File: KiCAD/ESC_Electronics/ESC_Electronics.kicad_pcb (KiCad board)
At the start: 2 copper layers, 57 parts, among them J1 -1000VDC, J2 Test Input, J3 CA probe, J4 DC Power, J5 Output, J6 Barrel_Jack, Q1 MMBT3906, Q2 MMBT3904, U1 CR110, U2 SiPhotodiode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

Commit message: laying out V1
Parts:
- added H1: MountingHole, MountingHole:MountingHole_3.2mm_M3, F.Cu at (195.6, 66.0)
- added H2: MountingHole, MountingHole:MountingHole_3.2mm_M3, F.Cu at (195.6, 124.5)
- added H3: MountingHole, MountingHole:MountingHole_3.2mm_M3, F.Cu at (79.0, 63.2)
- added H4: MountingHole, MountingHole:MountingHole_3.2mm_M3, F.Cu at (55.9, 124.5)
- added J7: -6V, Connector_PinHeader_2.54mm:PinHeader_1x02_P2.54mm_Vertical, F.Cu at (108.2, 120.6)
- added J8: +6V, Connector_PinHeader_2.54mm:PinHeader_1x02_P2.54mm_Vertical, F.Cu at (108.2, 106.4)
- added TH1: PTC 200mA, Fuse:Fuse_1210_3225Metric_Pad1.42x2.65mm_HandSolder, F.Cu at (64.8, 96.8)
- moved R4 115.4 mm to (133.6, 106.2)
- moved C4 111.7 mm to (74.2, 83.3), turned to 90 degrees
- moved R3 102.9 mm to (133.6, 101.1)
- moved BT6 97.4 mm to (136.4, 117.3), turned to 180 degrees
- moved R5 86.4 mm to (146.3, 70.6), turned to 0 degrees
- moved J4 85.4 mm to (84.5, 119.3), turned to 180 degrees
- moved D2 81.4 mm to (91.7, 121.7), turned to 0 degrees
- moved D1 79.7 mm to (91.7, 116.3), turned to 180 degrees
- moved R8 77.8 mm to (146.3, 65.7), turned to 0 degrees
- moved BT2 77.2 mm to (185.9, 91.7), turned to 90 degrees
- moved J3 71.6 mm to (93.2, 64.0), turned to -90 degrees
- moved U2 69.3 mm to (132.1, 84.6), turned to -90 degrees
- moved D5 67.9 mm to (103.1, 113.0)
- moved R6 66.6 mm to (131.1, 65.5), turned to 0 degrees
- moved BT5 65.3 mm to (171.4, 91.7), turned to 90 degrees
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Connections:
- L1 pad 1: Net-(J6-Pad1) -> Net-(L1-Pad1)
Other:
- rule pad_to_mask_clearance: 0 -> 0.0508
- board text added: "HV"
- board text added: "Output"
- board text added: "Test"

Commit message: layed out board
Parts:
- added H5: DiodeFeedThru, ESC_Electronics_Library:DiodeFeedThru, F.Cu at (118.7, 89.4)
- added R20: 10k, Resistor_THT:R_Axial_DIN0207_L6.3mm_D2.5mm_P5.08mm_Vertical, F.Cu at (108.0, 77.0)
- C6: value 1nF -> 1pF
- R11: footprint Resistor_SMD:R_0805_2012Metric_Pad1.20x1.40mm_HandSolder -> Resistor_THT:R_Axial_DIN0207_L6.3mm_D2.5mm_P5.08mm_Vertical
- R12: value 20k -> 10k; footprint Resistor_SMD:R_0805_2012Metric_Pad1.20x1.40mm_HandSolder -> Resistor_THT:R_Axial_DIN0207_L6.3mm_D2.5mm_P5.08mm_Vertical
- moved R11 6.66 mm to (93.5, 79.5), turned to -90 degrees
- moved R12 6.38 mm to (98.0, 77.0), turned to 0 degrees
- moved H1 6.04 mm to (195.5, 60.0)
- moved H3 4.24 mm to (77.0, 59.5)
- moved C12 3.42 mm to (103.1, 103.0)
- moved R18 2.62 mm to (103.1, 106.5)
- moved U3 1.52 mm to (106.4, 83.3)
- moved C9 1.13 mm to (105.5, 94.0)
- moved D6 0.71 mm to (103.2, 99.5)
- moved D5 0.47 mm to (103.1, 113.5)
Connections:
- C9 pad 2: Net-(C9-Pad2) -> GND
- R12 pad 1: Net-(J5-Pad1) -> GND
- R12 pad 2: Net-(R11-Pad2) -> Net-(R12-Pad2)
- U3 pad 2: Net-(C9-Pad2) -> Net-(R12-Pad2)
- U3 pad 4: Net-(C9-Pad2) -> GND
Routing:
- net Net-(R3-Pad2): track 0.00 -> 96.5 mm
- net Net-(C2-Pad1): track 0.00 -> 80.2 mm
- net -6VDC: track 0.00 -> 70.4 mm, vias 0 -> 2
- net Net-(C10-Pad2): track 0.00 -> 69.9 mm, vias 0 -> 1
- net +6VDC: track 0.00 -> 62.2 mm
- net Net-(BT2-Pad1): track 0.00 -> 42.8 mm
- net Net-(C10-Pad1): track 0.00 -> 40.5 mm
- net Net-(BT1-Pad2): track 0.00 -> 39.2 mm
- net Net-(BT2-Pad2): track 0.00 -> 37.7 mm
- net Net-(BT1-Pad1): track 0.00 -> 37.7 mm
- net Net-(BT3-Pad1): track 0.00 -> 37.7 mm
- net Net-(C5-Pad1): track 0.00 -> 36.3 mm
- net Net-(C8-Pad1): track 0.00 -> 26.7 mm
- net Net-(J5-Pad1): track 0.00 -> 23.3 mm
- net Net-(D1-Pad1): track 0.00 -> 22.8 mm, vias 0 -> 2
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- added copper zone on B.Cu, net GND
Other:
- board outline added: 149.5 x 74.5 mm
- board text added: "+6V GND"
- board text added: "+8V GND -8V"
- board text added: "-6V GND"
- board text added: "100uH"
- board text added: "1uF"
- board text added: "200mA PTC"
- board text added: "24VDC -Floating+"
- board text added: "BIAS IN"
- board text added: "GND"
- board text added: "LM317"
- board text added: "PreAmp Output"
- board text added: "TL072"
- board text added: "TLE2426"

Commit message: uploaded this version to OSHpark as V1
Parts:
- added H6: MountingHole, ESC_Electronics_Library:4headclear, F.Cu at (118.7, 108.4)
- added H7: MountingHole, ESC_Electronics_Library:4headclear, F.Cu at (118.7, 70.3)
- C1, C4: footprint Capacitor_SMD:C_1206_3216Metric_Pad1.33x1.80mm_HandSolder -> Capacitor_SMD:C_0805_2012Metric_Pad1.18x1.45mm_HandSolder
- R18, R19: footprint Resistor_SMD:R_0805_2012Metric_Pad1.20x1.40mm_HandSolder -> Resistor_SMD:R_1206_3216Metric_Pad1.30x1.75mm_HandSolder
- moved R6 6.37 mm to (136.9, 63.0)
- moved C7 5.51 mm to (134.1, 70.1)
- moved C3 5.20 mm to (126.5, 63.5)
- moved BT4 3.05 mm to (173.2, 120.4)
- moved BT6 3.05 mm to (136.4, 120.4)
- moved R5 2.03 mm to (148.3, 70.6)
- moved R8 2.03 mm to (148.3, 65.7)
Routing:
- net Net-(BT1-Pad2): track 39.2 -> 45.7 mm
- net Net-(C2-Pad1): track 80.2 -> 84.5 mm
- net Net-(BT2-Pad1): track 42.8 -> 45.9 mm
- net Net-(R3-Pad2): track 96.5 -> 99.2 mm
- net Net-(C5-Pad1): track 36.3 -> 34.2 mm
- net Net-(J1-Pad1): track 8.39 -> 6.36 mm
- net Net-(C3-Pad2): track 4.32 -> 5.58 mm
- net Net-(BT6-Pad1): track 19.9 -> 21.1 mm
- net Net-(D2-Pad2): track 16.1 -> 15.3 mm
- net Net-(D1-Pad1): track 22.8 -> 22.3 mm
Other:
- board text added: "Input Only"

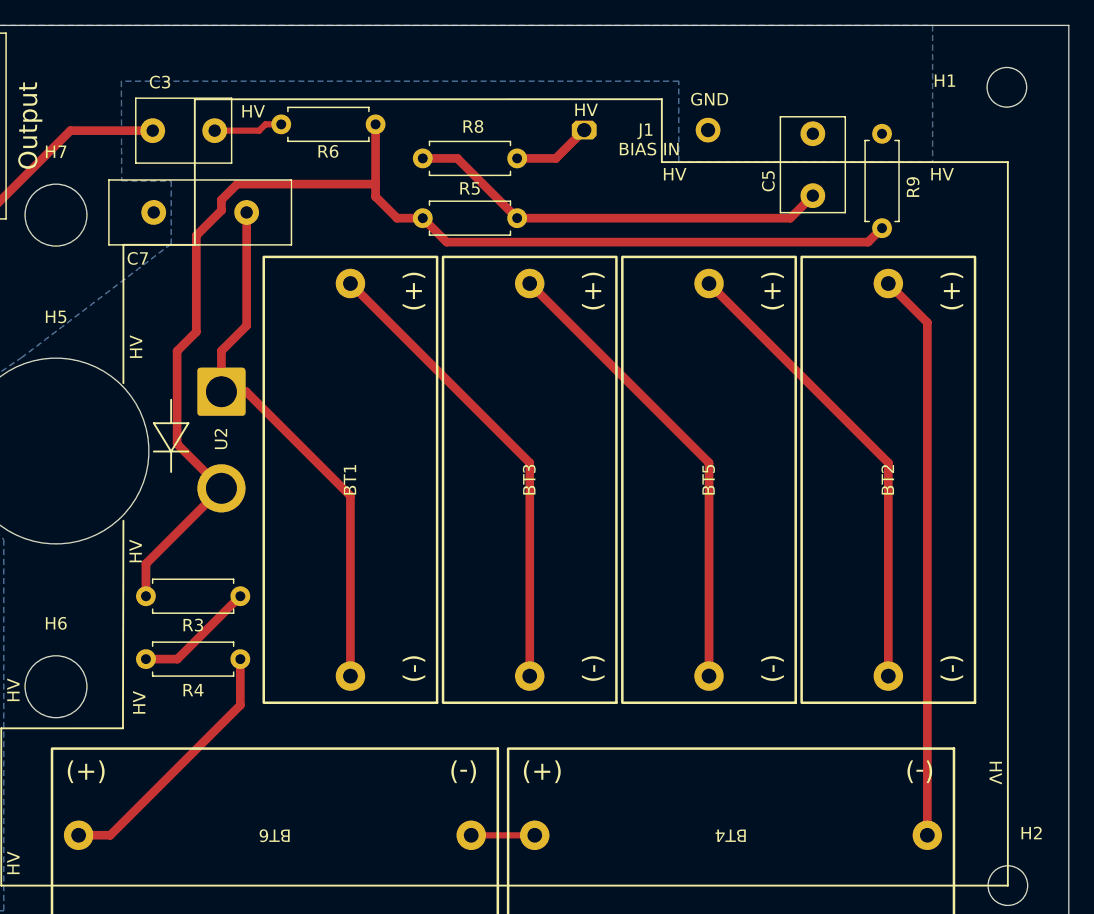
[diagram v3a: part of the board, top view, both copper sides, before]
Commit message: the real ESC V1
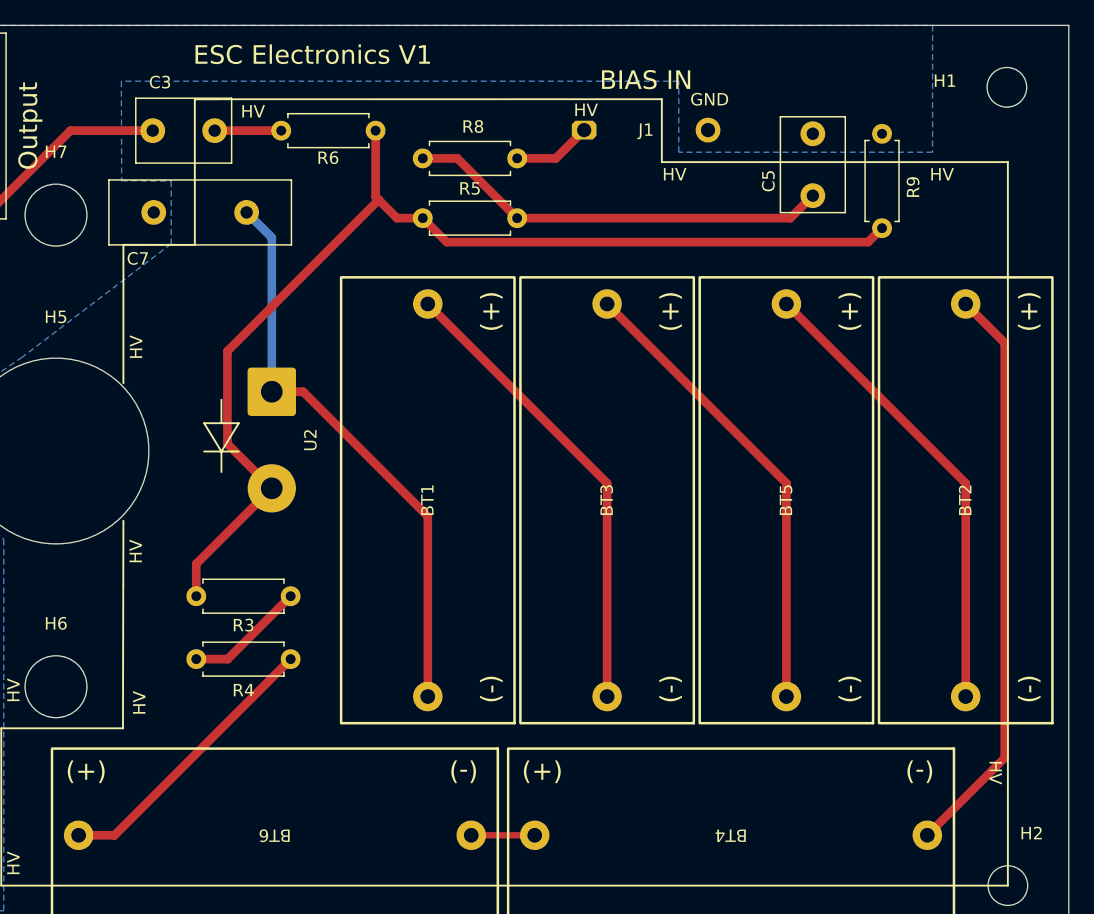
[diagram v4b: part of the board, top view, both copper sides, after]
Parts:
- U2: footprint Connector_Wire:SolderWire-2sqmm_1x02_P7.8mm_D2mm_OD3.9mm -> Connector_Wire:SolderWire-1sqmm_1x02_P7.8mm_D1.4mm_OD3.9mm
- moved BT5 6.46 mm to (177.7, 93.3)
- moved BT1 6.46 mm to (148.7, 93.3)
- moved BT2 6.46 mm to (192.2, 93.3)
- moved BT3 6.46 mm to (163.2, 93.3)
- moved R3 4.06 mm to (137.7, 101.1)
- moved R4 4.06 mm to (137.7, 106.2)
- moved U2 4.06 mm to (136.1, 84.6)
- moved R6 0.51 mm to (136.9, 63.5)
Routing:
- net Net-(R3-Pad2): track 99.2 -> 89.3 mm
- net Net-(BT1-Pad2): track 45.7 -> 48.6 mm
- net Net-(BT6-Pad1): track 21.1 -> 23.0 mm
- net Net-(BT2-Pad1): track 45.9 -> 46.8 mm
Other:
- board text added: "ESC Electronics V1"

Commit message: Refining for V2 while debugging
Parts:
- added C13: 0.1uF, Capacitor_SMD:C_0805_2012Metric_Pad1.18x1.45mm_HandSolder, F.Cu at (87.5, 97.0)
- D5, D6: value MM3Z6V8 -> MM3Z7V5T1G
- J6: footprint Connector_Wire:SolderWire-0.75sqmm_1x02_P7mm_D1.25mm_OD3.5mm -> Connector_Wire:SolderWire-0.25sqmm_1x02_P4.2mm_D0.65mm_OD1.7mm
- R11, R12, R20: footprint Resistor_THT:R_Axial_DIN0207_L6.3mm_D2.5mm_P5.08mm_Vertical -> Resistor_THT:R_Axial_DIN0207_L6.3mm_D2.5mm_P10.16mm_Horizontal
- U2: footprint Connector_Wire:SolderWire-1sqmm_1x02_P7.8mm_D1.4mm_OD3.9mm -> Connector_Wire:SolderWire-0.25sqmm_1x02_P4.2mm_D0.65mm_OD1.7mm
- moved U5 20.7 mm to (82.5, 116.0)
- moved R20 17.9 mm to (90.4, 80.5)
- moved D1 15.7 mm to (78.0, 124.0)
- moved D2 14.5 mm to (78.0, 126.5)
- moved J4 14.2 mm to (71.5, 125.0)
- moved U3 12.0 mm to (98.3, 92.2)
- moved R12 11.8 mm to (90.4, 86.0)
- moved C1 10.8 mm to (80.0, 89.5), turned to -90 degrees
- moved Q2 10.6 mm to (99.2, 106.9)
- moved R16 10.6 mm to (89.0, 106.9)
- moved C12 10.6 mm to (94.1, 108.6)
- moved D3 10.6 mm to (89.0, 112.0)
- moved D6 10.6 mm to (94.2, 105.1), turned to 180 degrees
- moved J8 10.6 mm to (99.2, 112.0), turned to 90 degrees
- moved R18 10.6 mm to (94.1, 112.1)
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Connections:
- D6 pad 1: GND -> Net-(C12-Pad1)
- D6 pad 2: Net-(C12-Pad1) -> GND
- U3 pad 4: GND -> -6VDC
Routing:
- net Net-(C10-Pad2): track 69.9 -> 54.6 mm, vias 1 -> 0
- net Net-(J5-Pad1): track 23.3 -> 31.4 mm
- net Net-(C10-Pad1): track 40.5 -> 33.0 mm
- net Net-(R12-Pad2): track 11.6 -> 18.7 mm
- net +6VDC: track 62.5 -> 57.1 mm
- net Net-(D2-Pad2): track 15.3 -> 20.2 mm
- net Net-(R7-Pad2): track 9.35 -> 13.7 mm
- net -6VDC: track 70.7 -> 74.9 mm
- net Net-(D1-Pad1): track 22.3 -> 26.5 mm
- net GND: track 19.3 -> 23.1 mm, vias 8 -> 9
- net Net-(R2-Pad2): track 7.82 -> 11.4 mm
- net Net-(J3-Pad1): track 16.0 -> 19.1 mm
- net Net-(R11-Pad2): track 10.9 -> 8.51 mm
- net Net-(C2-Pad1): track 84.5 -> 86.6 mm
- net Net-(L1-Pad2): track 10.6 -> 8.63 mm
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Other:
- board text added: "!!HIGH VOLTAGE!!"
- board text added: "ESC Electronics V2"
- board text removed: "ESC Electronics V1"

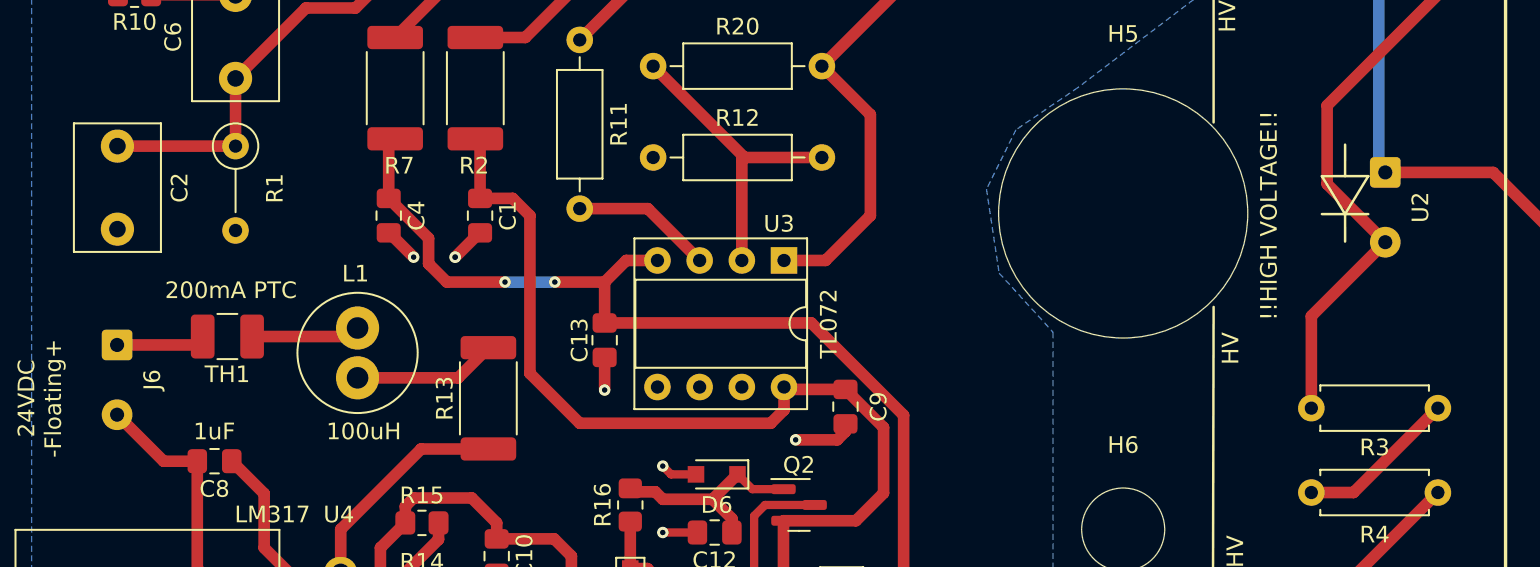
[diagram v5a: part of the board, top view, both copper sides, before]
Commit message: Refining for V2 while debugging R2
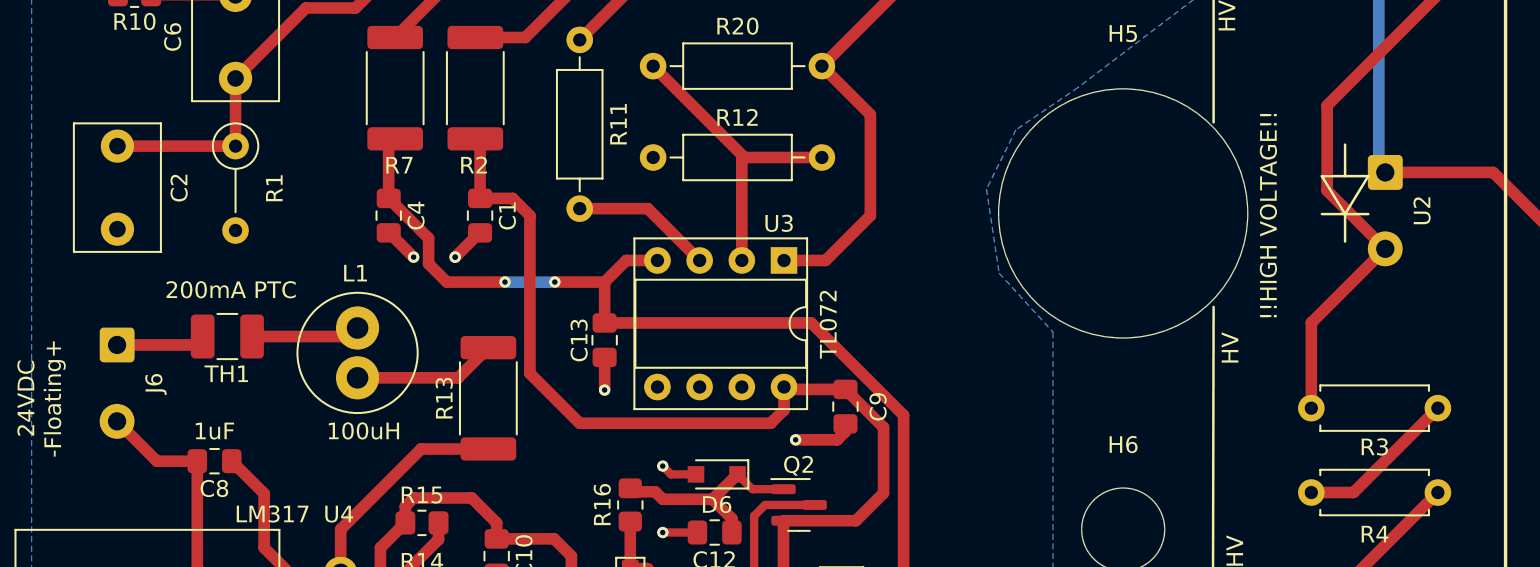
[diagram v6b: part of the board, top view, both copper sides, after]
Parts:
- J6, U2: footprint Connector_Wire:SolderWire-0.25sqmm_1x02_P4.2mm_D0.65mm_OD1.7mm -> Connector_Wire:SolderWire-0.5sqmm_1x02_P4.6mm_D0.9mm_OD2.1mm

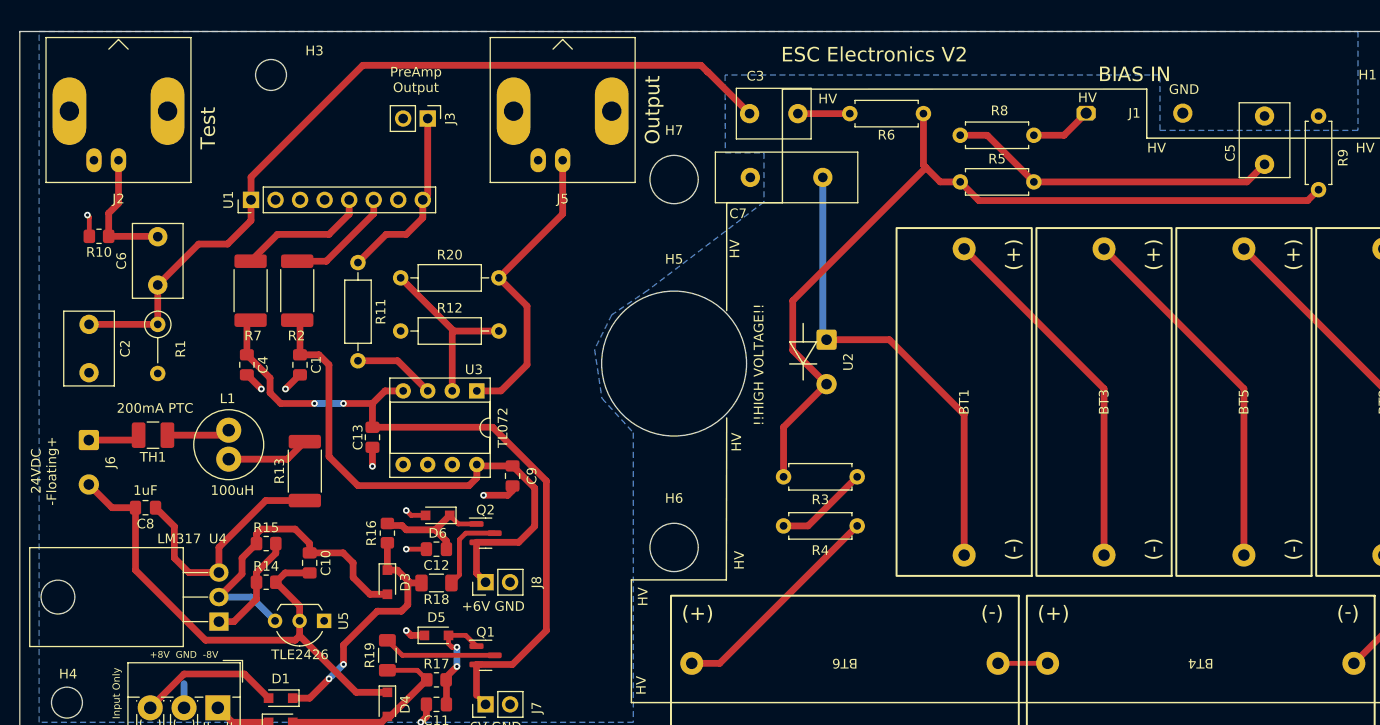
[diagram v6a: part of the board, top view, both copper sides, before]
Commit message: Refining for V2 while debugging R3
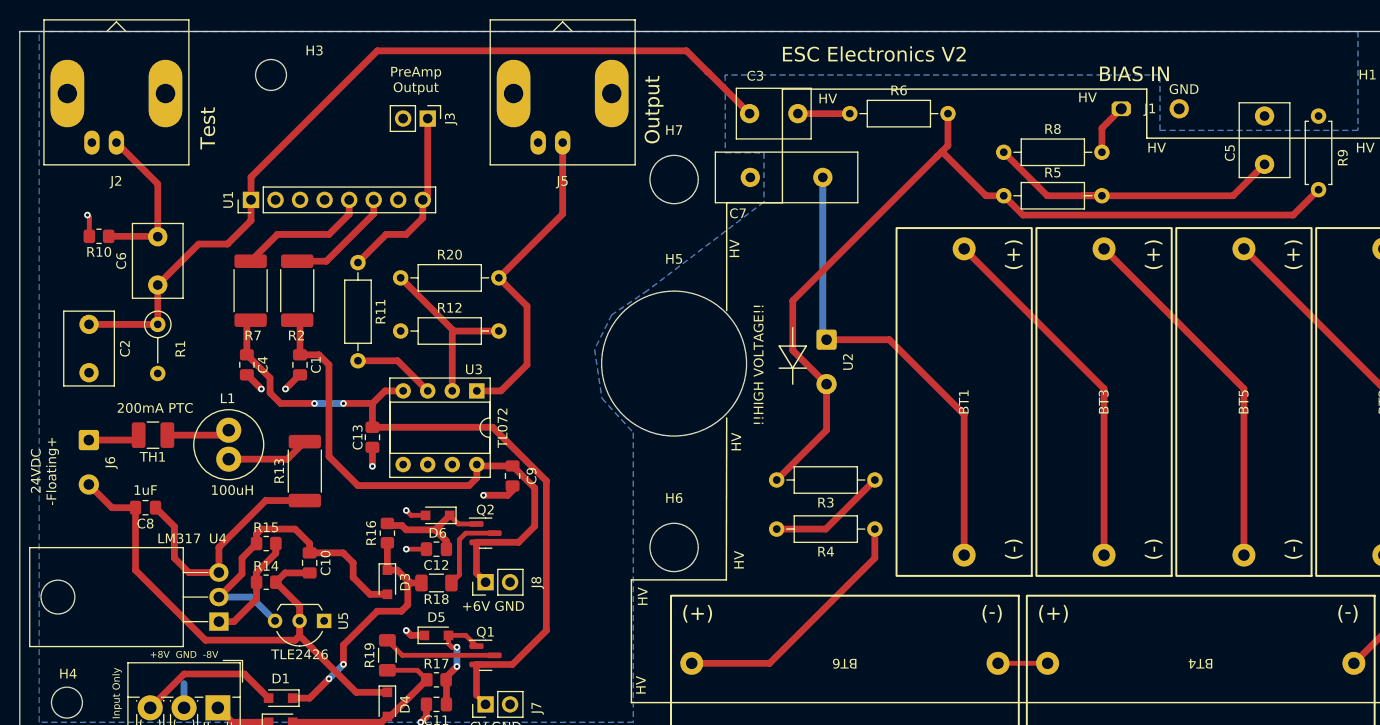
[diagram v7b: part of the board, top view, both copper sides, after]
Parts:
- R3, R4, R5, R6, R8: footprint Resistor_THT:R_Axial_DIN0207_L6.3mm_D2.5mm_P7.62mm_Horizontal -> Resistor_THT:R_Axial_DIN0207_L6.3mm_D2.5mm_P10.16mm_Horizontal
- moved R8 4.84 mm to (152.8, 67.5)
- moved R5 4.73 mm to (152.8, 72.0)
- moved R3 1.86 mm to (139.5, 101.4)
- moved R4 1.86 mm to (139.5, 106.5)
- moved J2 1.84 mm to (61.0, 66.5)
- moved J5 1.83 mm to (107.2, 66.5)
- moved J1 1.69 mm to (168.0, 63.0)
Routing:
- net Net-(BT6-Pad1): track 23.0 -> 26.5 mm
- net Net-(C6-Pad2): track 13.4 -> 16.6 mm
- net Net-(R3-Pad1): track 9.72 -> 12.3 mm
- net Net-(C5-Pad1): track 34.2 -> 32.1 mm
- net Net-(J5-Pad1): track 31.4 -> 33.3 mm
- net Net-(R3-Pad2): track 89.2 -> 91.0 mm
- net Net-(C2-Pad1): track 86.6 -> 87.8 mm
- net Net-(J1-Pad1): track 6.36 -> 5.33 mm

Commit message: Refining for V2 while debugging R4
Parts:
- added J9: Batt probe, Connector_PinHeader_2.54mm:PinHeader_1x02_P2.54mm_Vertical, F.Cu at (142.5, 127.5)
- C3, C5: footprint Capacitor_THT:C_Disc_D7.5mm_W5.0mm_P5.00mm -> Capacitor_THT:C_Disc_D10.5mm_W5.0mm_P7.50mm
- moved C5 5.00 mm to (179.8, 63.8), turned to -90 degrees
- moved R6 3.51 mm to (140.4, 63.5)
- moved J1 2.00 mm to (170.0, 63.0)
- moved R5 2.00 mm to (154.8, 72.0)
- moved R8 2.00 mm to (154.8, 67.5)
- moved BT6 1.52 mm to (137.0, 119.0)
- moved BT4 1.42 mm to (173.5, 119.0)
- moved D5 0.50 mm to (94.1, 117.0)
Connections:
- C5 pad 1: Net-(C5-Pad1) -> GND
- C5 pad 2: GND -> Net-(R5-Pad2)
- R5 pad 2: Net-(C5-Pad1) -> Net-(R5-Pad2)
- R8 pad 1: Net-(C5-Pad1) -> Net-(R5-Pad2)
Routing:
- net Net-(C5-Pad1): track 32.1 -> 0.00 mm
- net Net-(R5-Pad2): track 0.00 -> 27.1 mm
- net Net-(BT1-Pad2): track 49.0 -> 68.8 mm
- net Net-(BT6-Pad1): track 26.5 -> 42.5 mm
- net GND: track 23.1 -> 21.3 mm
- net Net-(C3-Pad2): track 5.37 -> 6.39 mm
- net Net-(BT2-Pad1): track 46.8 -> 45.9 mm
- net Net-(R3-Pad2): track 91.0 -> 91.5 mm
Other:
- board text added: "-1kV"
- board text added: "0 Ohm"
- board text added: "1000pF"
- board text added: "100M"
- board text added: "10M"
- board text added: "1nF"
- board text added: "1pF"
- board text added: "4700pF"
- board text added: "A = 1+R20/R12"
- board text added: "Batt +"
- board text added: "DIODE"
- board text added: "Test Input"
- board text added: "open"
- board text removed: "Test"
